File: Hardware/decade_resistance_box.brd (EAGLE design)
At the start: 101.6 x 76.2 mm, 61 parts, among them SW1 SWITCH_ROTARY_1X10KIT, SW2 SWITCH_ROTARY_1X10KIT, SW3 SWITCH_ROTARY_1X10KIT, SW4 SWITCH_ROTARY_1X10KIT, SW5 SWITCH_ROTARY_1X10KIT

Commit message: Updates from Prototype review
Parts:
- moved FRAME1 14.2 mm to (22.9, -24.1)
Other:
- board text added: "V10"
- board text removed: "V01"
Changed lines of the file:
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@@
 <layer number="27" name="tValues" color="7" fill="1" visible="no" active="yes"/>
 <layer number="28" name="bValues" color="7" fill="1" visible="no" active="yes"/>
-<layer number="29" name="tStop" color="7" fill="3" visible="no" active="yes"/>
-<layer number="30" name="bStop" color="7" fill="6" visible="no" active="yes"/>
+<layer number="29" name="tStop" color="7" fill="3" visible="yes" active="yes"/>
+<layer number="30" name="bStop" color="7" fill="6" visible="yes" active="yes"/>
 <layer number="31" name="tCream" color="7" fill="4" visible="no" active="yes"/>
 <layer number="32" name="bCream" color="7" fill="5" visible="no" active="yes"/>
@@
 <wire x1="98.0079" y1="76.2" x2="3.5921" y2="76.2" width="0.2032" layer="20"/>
 <wire x1="3.5921" y1="76.2" x2="0" y2="72.6079" width="0.2032" layer="20" curve="90"/>
-<text x="46.99" y="-10.16" size="1.778" layer="51" font="vector" ratio="15">Byron Jacquot</text>
+<text x="50.8" y="-24.13" size="1.778" layer="51" font="vector" ratio="15">Byron Jacquot</text>
 <wire x1="0" y1="26.67" x2="101.6" y2="26.67" width="0.254" layer="51"/>
 <wire x1="0" y1="60.96" x2="101.6" y2="60.96" width="0.254" layer="51"/>
@@
 <wire x1="17.78" y1="76.2" x2="17.78" y2="0" width="0.254" layer="51"/>
 <wire x1="83.82" y1="76.2" x2="83.82" y2="0" width="0.254" layer="51"/>
-<text x="6.35" y="2.54" size="1.778" layer="16" font="vector" ratio="15" rot="MR180">V01</text>
+<text x="6.35" y="2.54" size="1.778" layer="16" font="vector" ratio="15" rot="MR180">V10</text>
 <text x="50.8" y="29.21" size="2.54" layer="21" font="vector" ratio="15" align="top-center">Decade
 Resistance
@@
 <hole x="50.8" y="60.96" drill="3.81"/>
 <hole x="83.82" y="60.96" drill="3.81"/>
+<hole x="3.81" y="12.7" drill="3.81"/>
+<hole x="80.01" y="26.67" drill="3.81"/>
+<wire x1="0" y1="76.2" x2="0" y2="8.89" width="0.254" layer="51"/>
+<wire x1="0" y1="8.89" x2="0" y2="0" width="0.254" layer="51"/>
+<wire x1="101.6" y1="76.2" x2="101.6" y2="8.89" width="0.254" layer="51"/>
+<wire x1="101.6" y1="8.89" x2="101.6" y2="0" width="0.254" layer="51"/>
+<wire x1="0" y1="76.2" x2="101.6" y2="76.2" width="0.254" layer="51"/>
+<wire x1="0" y1="0" x2="41.275" y2="0" width="0.254" layer="51"/>
+<wire x1="41.275" y1="0" x2="60.325" y2="0" width="0.254" layer="51"/>
+<wire x1="60.325" y1="0" x2="101.6" y2="0" width="0.254" layer="51"/>
+<wire x1="0" y1="8.89" x2="101.6" y2="8.89" width="0.254" layer="51"/>
+<dimension x1="0" y1="0" x2="0" y2="8.89" x3="-3.81" y3="4.445" textsize="1.778" textratio="15" layer="51" unit="inch"/>
+<dimension x1="0" y1="0" x2="0" y2="26.67" x3="-7.62" y3="13.335" textsize="1.778" textratio="15" layer="51" unit="inch"/>
+<dimension x1="0" y1="0" x2="0" y2="60.96" x3="-11.43" y3="30.48" textsize="1.778" textratio="15" layer="51" unit="inch"/>
+<wire x1="60.325" y1="20.32" x2="60.325" y2="0" width="0.254" layer="51"/>
+<wire x1="41.275" y1="20.32" x2="41.275" y2="0" width="0.254" layer="51"/>
+<dimension x1="0" y1="0" x2="41.275" y2="0" x3="20.6375" y3="-8.89" textsize="1.778" textratio="15" layer="51" unit="inch" precision="3"/>
+<dimension x1="41.275" y1="0" x2="60.325" y2="0" x3="50.8" y3="-8.89" textsize="1.778" textratio="15" layer="51" unit="inch" precision="3"/>
+<dimension x1="0" y1="0" x2="21.59" y2="0" x3="10.795" y3="-3.81" textsize="1.778" textratio="15" layer="51" unit="inch" precision="3"/>
+<dimension x1="0" y1="0" x2="80.01" y2="0" x3="40.005" y3="-13.97" textsize="1.778" textratio="15" layer="51" unit="inch" precision="3"/>
+<dimension x1="0" y1="76.2" x2="17.78" y2="76.2" x3="8.89" y3="80.01" textsize="1.778" textratio="15" layer="51" unit="inch" precision="3"/>
+<dimension x1="0" y1="76.2" x2="50.8" y2="76.2" x3="25.4" y3="83.82" textsize="1.778" textratio="15" layer="51" unit="inch" precision="3"/>
+<dimension x1="0" y1="76.2" x2="83.82" y2="76.2" x3="41.91" y3="87.63" textsize="1.778" textratio="15" layer="51" unit="inch" precision="3"/>
 <hole x="21.59" y="26.67" drill="3.81"/>
-<hole x="80.01" y="26.67" drill="3.81"/>
+<hole x="3.81" y="31.75" drill="3.81"/>
 </plain>
 <attributes>
@@
 </autorouter>
 <elements>
-<element name="FRAME1" library="SparkFun-Aesthetics" package="CREATIVE_COMMONS" value="FRAME-LETTER" x="20.32" y="-10.16"/>
+<element name="FRAME1" library="SparkFun-Aesthetics" package="CREATIVE_COMMONS" value="FRAME-LETTER" x="22.86" y="-24.13"/>
 <element name="SW1" library="Testing" package="ROTARY_SWITCH_1X10_KIT" value="SWITCH_ROTARY_1X10KIT" x="17.78" y="60.96" rot="R270">
 <attribute name="PROD_ID" value="SWCH-12120" x="17.78" y="60.96" size="1.778" layer="27" rot="R270" display="off"/>

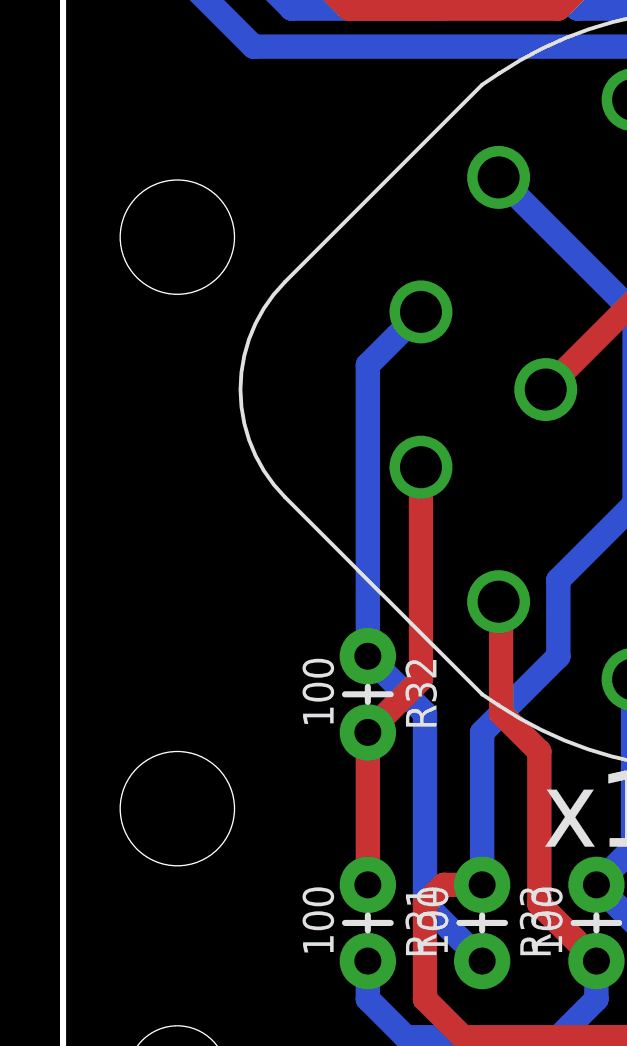
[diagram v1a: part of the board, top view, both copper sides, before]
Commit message: Updates following redboard review
Added a couple more dimension markings
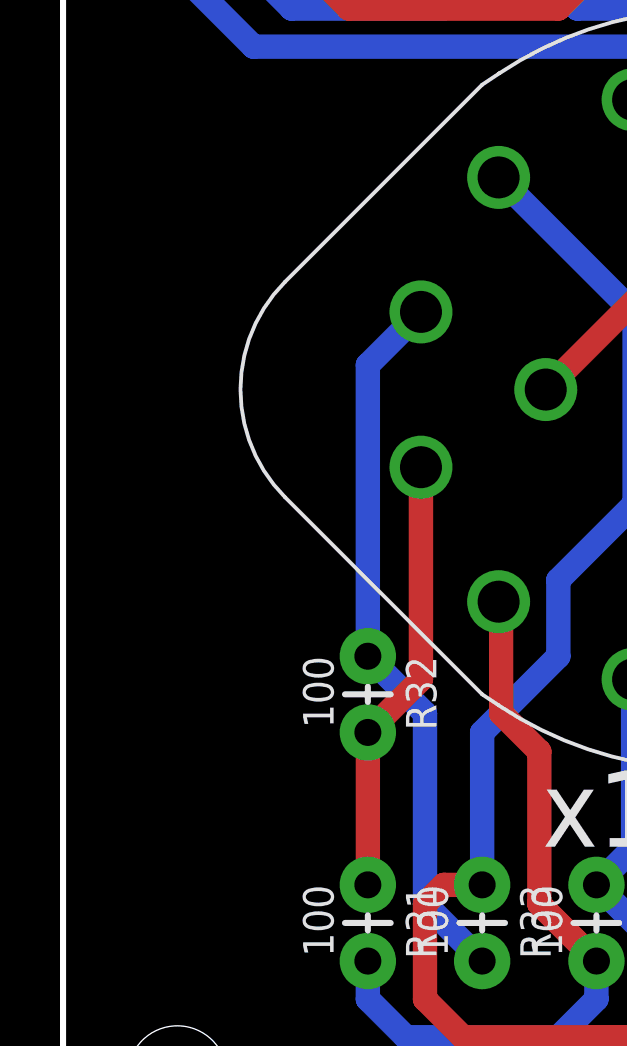
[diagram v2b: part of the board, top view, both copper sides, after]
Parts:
- moved FRAME1 8.98 mm to (24.1, -33.0)
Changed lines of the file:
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@@
 <layer number="27" name="tValues" color="7" fill="1" visible="no" active="yes"/>
 <layer number="28" name="bValues" color="7" fill="1" visible="no" active="yes"/>
-<layer number="29" name="tStop" color="7" fill="3" visible="yes" active="yes"/>
-<layer number="30" name="bStop" color="7" fill="6" visible="yes" active="yes"/>
+<layer number="29" name="tStop" color="7" fill="3" visible="no" active="yes"/>
+<layer number="30" name="bStop" color="7" fill="6" visible="no" active="yes"/>
 <layer number="31" name="tCream" color="7" fill="4" visible="no" active="yes"/>
 <layer number="32" name="bCream" color="7" fill="5" visible="no" active="yes"/>
@@
 <layer number="43" name="vRestrict" color="2" fill="10" visible="no" active="yes"/>
 <layer number="44" name="Drills" color="7" fill="1" visible="no" active="yes"/>
-<layer number="45" name="Holes" color="7" fill="1" visible="yes" active="yes"/>
+<layer number="45" name="Holes" color="7" fill="1" visible="no" active="yes"/>
 <layer number="46" name="Milling" color="3" fill="1" visible="no" active="yes"/>
 <layer number="47" name="Measures" color="7" fill="1" visible="no" active="yes"/>
@@
 <wire x1="98.0079" y1="76.2" x2="3.5921" y2="76.2" width="0.2032" layer="20"/>
 <wire x1="3.5921" y1="76.2" x2="0" y2="72.6079" width="0.2032" layer="20" curve="90"/>
-<text x="50.8" y="-24.13" size="1.778" layer="51" font="vector" ratio="15">Byron Jacquot</text>
+<text x="50.8" y="-33.02" size="1.778" layer="51" font="vector" ratio="15">Byron Jacquot</text>
 <wire x1="0" y1="26.67" x2="101.6" y2="26.67" width="0.254" layer="51"/>
 <wire x1="0" y1="60.96" x2="101.6" y2="60.96" width="0.254" layer="51"/>
@@
 <hole x="50.8" y="60.96" drill="3.81"/>
 <hole x="83.82" y="60.96" drill="3.81"/>
-<hole x="3.81" y="12.7" drill="3.81"/>
 <hole x="80.01" y="26.67" drill="3.81"/>
 <wire x1="0" y1="76.2" x2="0" y2="8.89" width="0.254" layer="51"/>
-<wire x1="0" y1="8.89" x2="0" y2="0" width="0.254" layer="51"/>
+<wire x1="0" y1="8.89" x2="0" y2="3.81" width="0.254" layer="51"/>
+<wire x1="0" y1="3.81" x2="0" y2="0" width="0.254" layer="51"/>
 <wire x1="101.6" y1="76.2" x2="101.6" y2="8.89" width="0.254" layer="51"/>
-<wire x1="101.6" y1="8.89" x2="101.6" y2="0" width="0.254" layer="51"/>
-<wire x1="0" y1="76.2" x2="101.6" y2="76.2" width="0.254" layer="51"/>
-<wire x1="0" y1="0" x2="41.275" y2="0" width="0.254" layer="51"/>
+<wire x1="101.6" y1="8.89" x2="101.6" y2="3.81" width="0.254" layer="51"/>
+<wire x1="101.6" y1="3.81" x2="101.6" y2="0" width="0.254" layer="51"/>
+<wire x1="0" y1="76.2" x2="3.81" y2="76.2" width="0.254" layer="51"/>
+<wire x1="3.81" y1="76.2" x2="101.6" y2="76.2" width="0.254" layer="51"/>
+<wire x1="0" y1="0" x2="3.81" y2="0" width="0.254" layer="51"/>
+<wire x1="3.81" y1="0" x2="41.275" y2="0" width="0.254" layer="51"/>
 <wire x1="41.275" y1="0" x2="60.325" y2="0" width="0.254" layer="51"/>
 <wire x1="60.325" y1="0" x2="101.6" y2="0" width="0.254" layer="51"/>
 <wire x1="0" y1="8.89" x2="101.6" y2="8.89" width="0.254" layer="51"/>
-<dimension x1="0" y1="0" x2="0" y2="8.89" x3="-3.81" y3="4.445" textsize="1.778" textratio="15" layer="51" unit="inch"/>
-<dimension x1="0" y1="0" x2="0" y2="26.67" x3="-7.62" y3="13.335" textsize="1.778" textratio="15" layer="51" unit="inch"/>
-<dimension x1="0" y1="0" x2="0" y2="60.96" x3="-11.43" y3="30.48" textsize="1.778" textratio="15" layer="51" unit="inch"/>
+<dimension x1="0" y1="0" x2="0" y2="8.89" x3="-7.62" y3="4.445" textsize="1.778" textratio="15" layer="51" unit="inch"/>
+<dimension x1="0" y1="0" x2="0" y2="26.67" x3="-11.43" y3="13.335" textsize="1.778" textratio="15" layer="51" unit="inch"/>
+<dimension x1="0" y1="0" x2="0" y2="60.96" x3="-15.24" y3="30.48" textsize="1.778" textratio="15" layer="51" unit="inch"/>
 <wire x1="60.325" y1="20.32" x2="60.325" y2="0" width="0.254" layer="51"/>
 <wire x1="41.275" y1="20.32" x2="41.275" y2="0" width="0.254" layer="51"/>
-<dimension x1="0" y1="0" x2="41.275" y2="0" x3="20.6375" y3="-8.89" textsize="1.778" textratio="15" layer="51" unit="inch" precision="3"/>
-<dimension x1="41.275" y1="0" x2="60.325" y2="0" x3="50.8" y3="-8.89" textsize="1.778" textratio="15" layer="51" unit="inch" precision="3"/>
-<dimension x1="0" y1="0" x2="21.59" y2="0" x3="10.795" y3="-3.81" textsize="1.778" textratio="15" layer="51" unit="inch" precision="3"/>
-<dimension x1="0" y1="0" x2="80.01" y2="0" x3="40.005" y3="-13.97" textsize="1.778" textratio="15" layer="51" unit="inch" precision="3"/>
+<dimension x1="0" y1="0" x2="41.275" y2="0" x3="20.6375" y3="-12.7" textsize="1.778" textratio="15" layer="51" unit="inch" precision="3"/>
+<dimension x1="41.275" y1="0" x2="60.325" y2="0" x3="50.8" y3="-12.7" textsize="1.778" textratio="15" layer="51" unit="inch" precision="3"/>
+<dimension x1="0" y1="0" x2="21.59" y2="0" x3="10.795" y3="-7.62" textsize="1.778" textratio="15" layer="51" unit="inch" precision="3"/>
+<dimension x1="0" y1="0" x2="80.01" y2="0" x3="40.005" y3="-17.78" textsize="1.778" textratio="15" layer="51" unit="inch" precision="3"/>
 <dimension x1="0" y1="76.2" x2="17.78" y2="76.2" x3="8.89" y3="80.01" textsize="1.778" textratio="15" layer="51" unit="inch" precision="3"/>
 <dimension x1="0" y1="76.2" x2="50.8" y2="76.2" x3="25.4" y3="83.82" textsize="1.778" textratio="15" layer="51" unit="inch" precision="3"/>
 <dimension x1="0" y1="76.2" x2="83.82" y2="76.2" x3="41.91" y3="87.63" textsize="1.778" textratio="15" layer="51" unit="inch" precision="3"/>
 <hole x="21.59" y="26.67" drill="3.81"/>
-<hole x="3.81" y="31.75" drill="3.81"/>
+<dimension x1="0" y1="0" x2="3.81" y2="0" x3="1.905" y3="-3.81" textsize="1.778" textratio="15" layer="51" unit="inch"/>
+<dimension x1="0" y1="0" x2="0" y2="3.81" x3="-3.81" y3="1.905" textsize="1.778" textratio="15" layer="51" unit="inch"/>
+<dimension x1="0" y1="0" x2="101.6" y2="0" x3="50.8" y3="-22.86" textsize="1.778" textratio="15" layer="51" unit="inch"/>
+<dimension x1="0" y1="0" x2="0" y2="76.2" x3="-19.05" y3="38.1" textsize="1.778" textratio="15" layer="51" unit="inch"/>
+<wire x1="0" y1="3.81" x2="101.6" y2="3.81" width="0.254" layer="51"/>
+<wire x1="3.81" y1="76.2" x2="3.81" y2="0" width="0.254" layer="51"/>
+<dimension x1="96.52" y1="73.533" x2="99.06" y2="71.247" x3="103.810190625" y3="79.079103125" textsize="1.778" textratio="15" layer="51" dtype="diameter" unit="inch" precision="3"/>
 </plain>
 <attributes>
@@
 </autorouter>
 <elements>
-<element name="FRAME1" library="SparkFun-Aesthetics" package="CREATIVE_COMMONS" value="FRAME-LETTER" x="22.86" y="-24.13"/>
+<element name="FRAME1" library="SparkFun-Aesthetics" package="CREATIVE_COMMONS" value="FRAME-LETTER" x="24.13" y="-33.02"/>
 <element name="SW1" library="Testing" package="ROTARY_SWITCH_1X10_KIT" value="SWITCH_ROTARY_1X10KIT" x="17.78" y="60.96" rot="R270">
 <attribute name="PROD_ID" value="SWCH-12120" x="17.78" y="60.96" size="1.778" layer="27" rot="R270" display="off"/>
